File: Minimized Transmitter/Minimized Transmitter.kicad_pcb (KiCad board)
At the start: 2 copper layers, 26 x 27.6 mm, 8 parts, among them J1 Conn_ARM_JTAG_SWD_10, J2 Conn_01x02_Male, J3 Conn_01x03_Male, U1 LPC824M201JHI33, U2 RFM69HCW

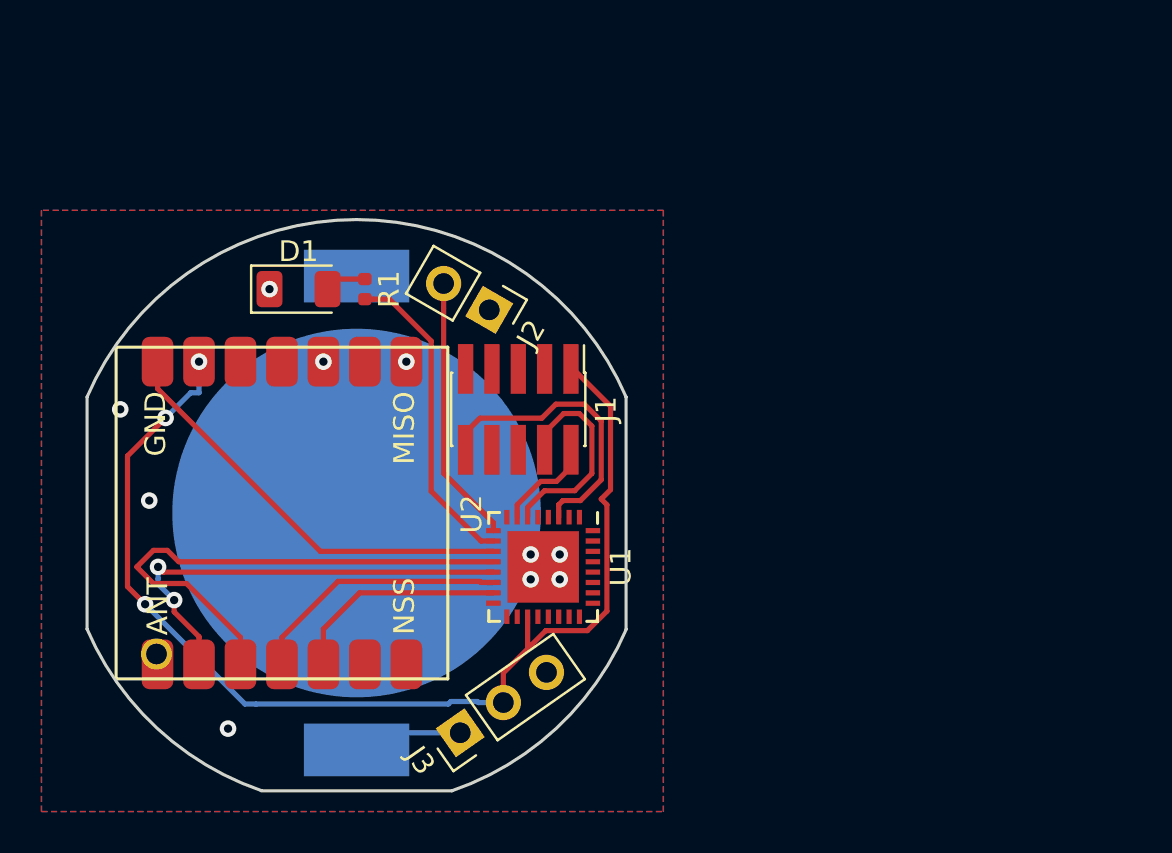
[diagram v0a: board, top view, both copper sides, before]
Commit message: Added some flat edges
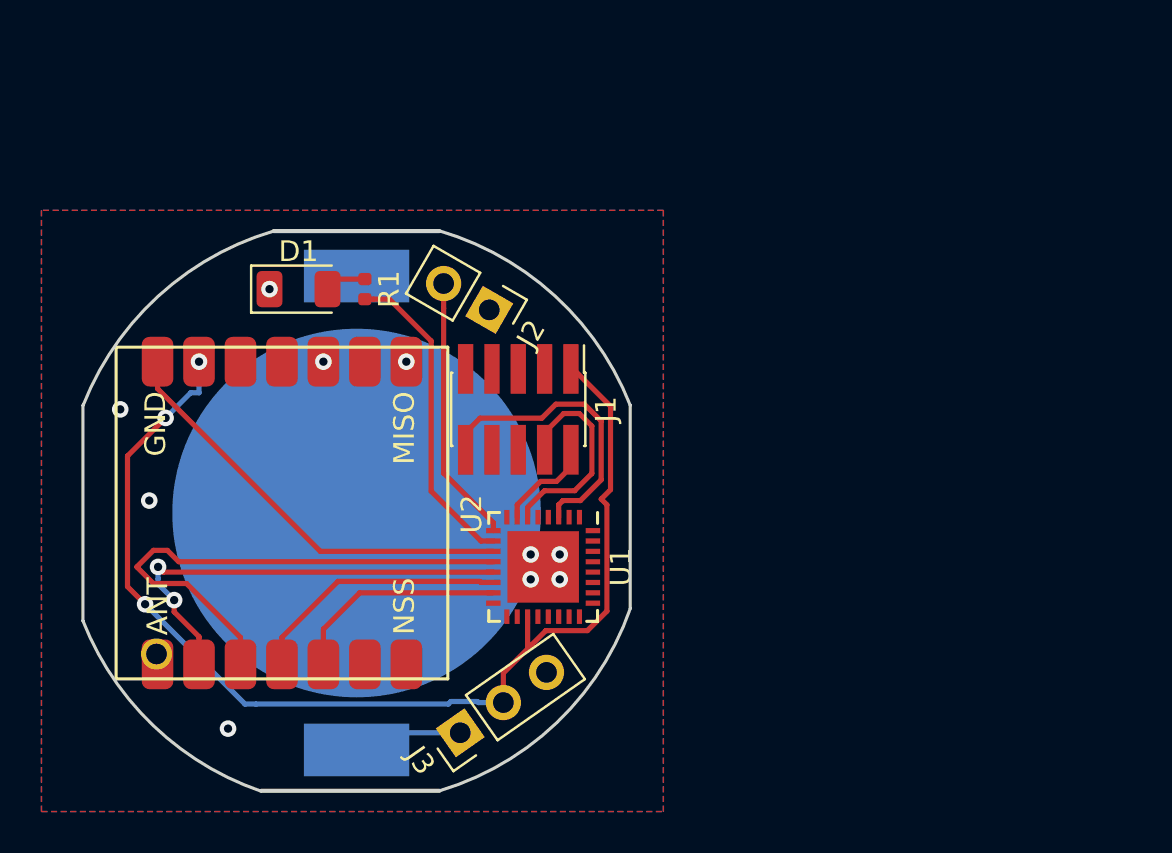
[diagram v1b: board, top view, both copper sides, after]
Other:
- board size 26 x 27.6 mm -> 26.4 x 27 mm
- board text added: "Disc Transmitter"
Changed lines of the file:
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@@
   (general
     (thickness 1.6)
-    (drawings 6)
+    (drawings 9)
     (tracks 107)
     (zones 0)
@@
     (pad_to_mask_clearance 0.2)
     (aux_axis_origin 0 0)
-    (visible_elements FFFFFF7F)
+    (visible_elements 7FFFFFFF)
     (pcbplotparams
       (layerselection 0x010fc_ffffffff)
@@
     )
   )
-  (gr_arc (start 163.2 77.6) (end 167.799999 90.999999) (angle -47.74860477) (layer Edge.Cuts) (width 0.15))
-  (gr_arc (start 163.2 77.6) (end 150.200001 83.199999) (angle -47.74860477) (layer Edge.Cuts) (width 0.15))
-  (gr_arc (start 163.2 77.6) (end 176.199999 72.000001) (angle -133.3902189) (layer Edge.Cuts) (width 0.15))
-  (gr_line (start 150.2 72) (end 150.2 83.2) (layer Edge.Cuts) (width 0.15))
-  (gr_line (start 176.2 83.2) (end 176.2 72) (layer Edge.Cuts) (width 0.15))
-  (gr_line (start 158.6 91) (end 167.8 91) (layer Edge.Cuts) (width 0.15))
+  (gr_text "Disc Transmitter\n" (at 151.8 77.6 90) (layer B.SilkS)
+    (effects (font (size 1.3 1) (thickness 0.25)) (justify mirror))
+  )
+  (gr_line (start 167.2 91) (end 158.6 91) (layer Edge.Cuts) (width 0.2))
+  (gr_line (start 150 82.8) (end 150 72.4) (layer Edge.Cuts) (width 0.15))
+  (gr_line (start 167.2 64) (end 159.2 64) (layer Edge.Cuts) (width 0.2))
+  (gr_arc (start 163.2 77.6) (end 159.2 64) (angle -52.10902466) (layer Edge.Cuts) (width 0.15))
+  (gr_arc (start 163.2 77.6) (end 176.4 72.4) (angle -52.10902625) (layer Edge.Cuts) (width 0.15))
+  (gr_arc (start 163.2 77.6) (end 167.2 91) (angle -54.16657326) (layer Edge.Cuts) (width 0.15))
+  (gr_arc (start 163.2 77.6) (end 150 82.8) (angle -49.55206173) (layer Edge.Cuts) (width 0.15))
+  (gr_line (start 176.4 82.2) (end 176.4 72.4) (layer Edge.Cuts) (width 0.15))
+  (segment (start 164.03 88.2) (end 163.2 89.03) (width 0.25) (layer B.Cu) (net 1))
+  (segment (start 168.2 88.2) (end 164.03 88.2) (width 0.25) (layer B.Cu) (net 1))
   (via (at 153.2 77) (size 0.8) (drill 0.4) (layers F.Cu B.Cu) (net 2))
   (via (at 157 88) (size 0.8) (drill 0.4) (layers F.Cu B.Cu) (net 2))
-  (segment (start 164.03 88.2) (end 163.2 89.03) (width 0.25) (layer B.Cu) (net 1))
-  (segment (start 168.2 88.2) (end 164.03 88.2) (width 0.25) (layer B.Cu) (net 1))
   (via (at 173 80.8) (size 0.8) (drill 0.4) (layers F.Cu B.Cu) (net 2))
   (via (at 171.6 80.8) (size 0.8) (drill 0.4) (layers F.Cu B.Cu) (net 2))

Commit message: Fixed pads on RFM footprint
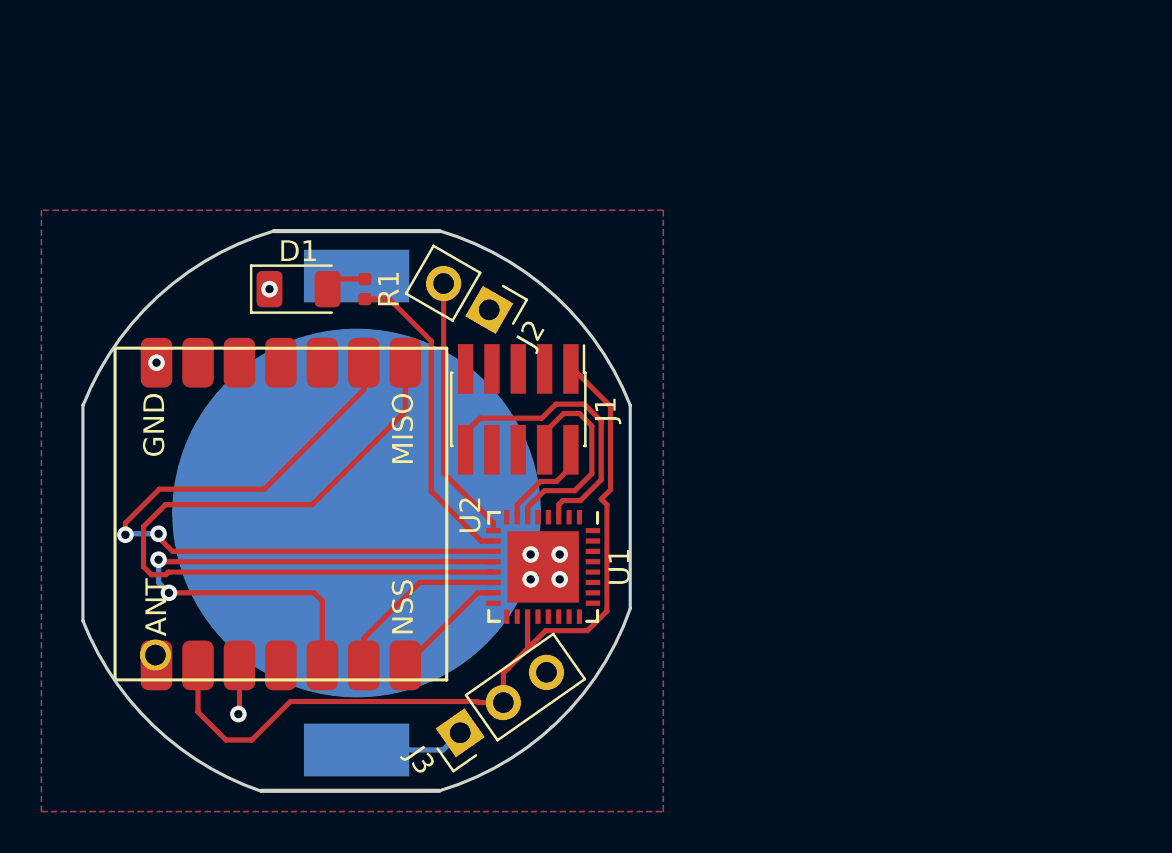
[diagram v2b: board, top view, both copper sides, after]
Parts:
- moved U2 0.07 mm to (159.6, 77.7)
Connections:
- U2 pad 10: GND -> Net-(U2-Pad10)
- U2 pad 13: +3V3 -> DIO0
- U2 pad 14: DIO0 -> MISO
- U2 pad 2: MISO -> +3V3
- U2 pad 3: MOSI -> GND
- U2 pad 4: SCK -> Net-(U2-Pad4)
- U2 pad 5: NSS -> MOSI
- U2 pad 6: Net-(U2-Pad6) -> SCK
- U2 pad 7: Net-(U2-Pad7) -> NSS
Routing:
- net +3V3: track 55.1 -> 40.4 mm, vias 3 -> 0
- net MISO: track 21.8 -> 36.3 mm, vias 2 -> 0
- net DIO0: track 20.8 -> 34.3 mm, vias 0 -> 2
- net NSS: track 10.6 -> 5.70 mm
- net SCK: track 12.6 -> 8.67 mm
- net MOSI: track 25.5 -> 28.7 mm, vias 0 -> 2
- net GND: track 0.00 -> 2.37 mm, vias 10 -> 7
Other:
- board text added: "GND"
- board text added: "TX"

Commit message: Added reset btn and removed on off switch
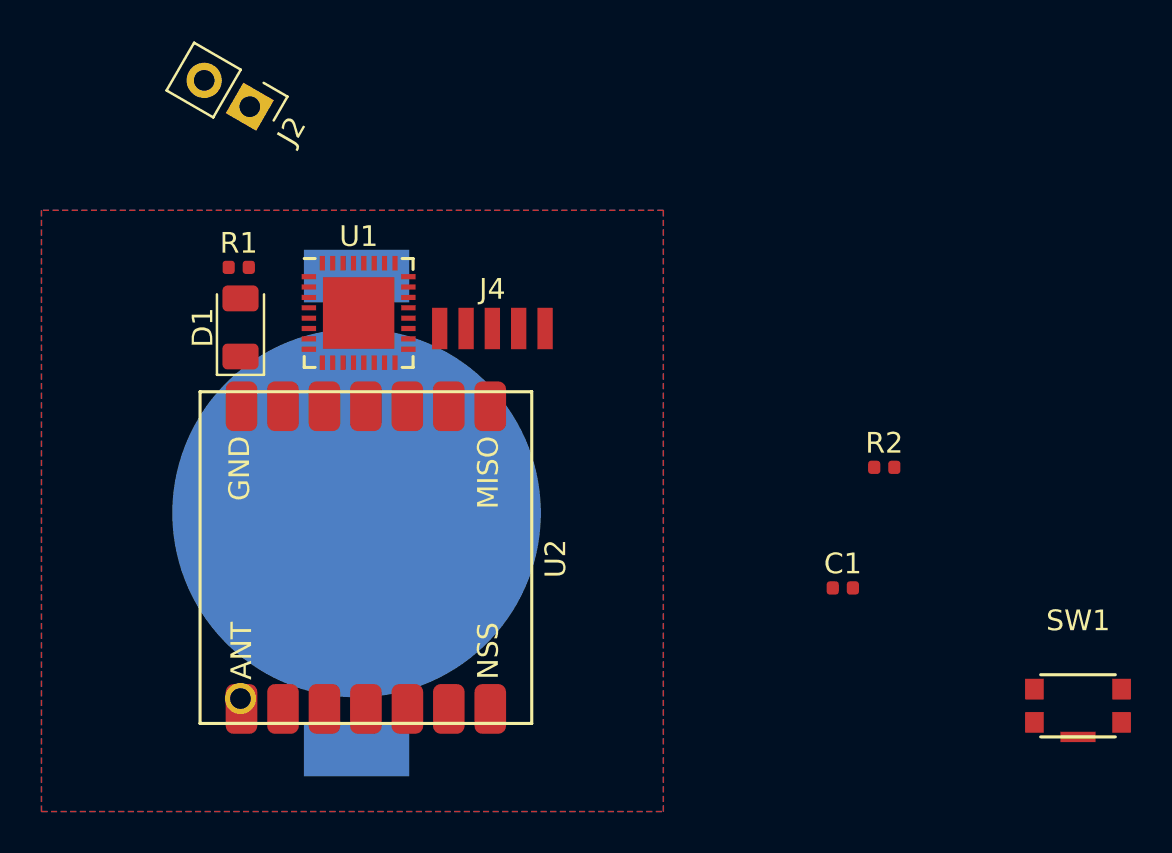
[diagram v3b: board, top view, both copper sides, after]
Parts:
- removed J1: Conn_ARM_JTAG_SWD_10, Connector_PinHeader_1.27mm:PinHeader_2x05_P1.27mm_Vertical_SMD
- removed J3: Conn_01x03_Male, Connector_PinHeader_2.54mm:PinHeader_1x03_P2.54mm_Vertical
- added C1: 0.1uF, Capacitor_SMD:C_0402_1005Metric, F.Cu at (186.7, 81.2)
- added J4: Conn_01x05_Male, my_foot_prints:SWD_5_Pin_Minimized_SurfaceMount, F.Cu at (169.8, 68.7)
- added R2: 100Kohms, Resistor_SMD:R_0402_1005Metric, F.Cu at (188.7, 75.4)
- added SW1: SW_Push, my_foot_prints:KMR221GLFS, F.Cu at (198.0, 86.9)
- moved J2 15.1 mm to (158.1, 58.0)
- moved U1 15.1 mm to (163.3, 68.0), turned to 0 degrees
- moved R1 6.17 mm to (157.5, 65.8), turned to 0 degrees
- moved U2 4.61 mm to (163.7, 79.8)
- moved D1 3.36 mm to (157.6, 68.7), turned to 90 degrees
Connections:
- BT1 pad 1: Net-(BT1-Pad1) -> +3V3
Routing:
- net +3V3: track 40.4 -> 0.00 mm
- net MISO: track 36.3 -> 0.00 mm
- net DIO0: track 34.3 -> 0.00 mm, vias 2 -> 0
- net MOSI: track 28.7 -> 0.00 mm, vias 2 -> 0
- net LED: track 15.3 -> 0.00 mm
- net nRESET: track 14.3 -> 0.00 mm
- net TX: track 12.9 -> 0.00 mm
- net SWDCLK: track 10.3 -> 0.00 mm
- net SCK: track 8.67 -> 0.00 mm
- net NSS: track 5.70 -> 0.00 mm
- net Net-(BT1-Pad1): track 5.34 -> 0.00 mm
- net SWDIO: track 4.77 -> 0.00 mm
- net GND: track 2.37 -> 0.00 mm, vias 7 -> 0
- net Net-(D1-Pad2): track 2.00 -> 0.00 mm
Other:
- board outline removed
